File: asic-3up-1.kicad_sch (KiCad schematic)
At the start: 79 parts, among them J14 Conn_01x01, J15 Conn_01x01, J5 Conn_01x01, J7 Conn_01x01, U48 MCP1824T-1202E/OT, U49 MCP1824T-1202E/OT, U50 MCP1824T-1202E/OT, U51 MCP1824T-0802E, U52 MCP1824T-0802E, U53 MCP1824T-0802E, U54 BM1362AC_MODE1, U55 BM1362AC_MODE0, U56 BM1362AC_MODE1

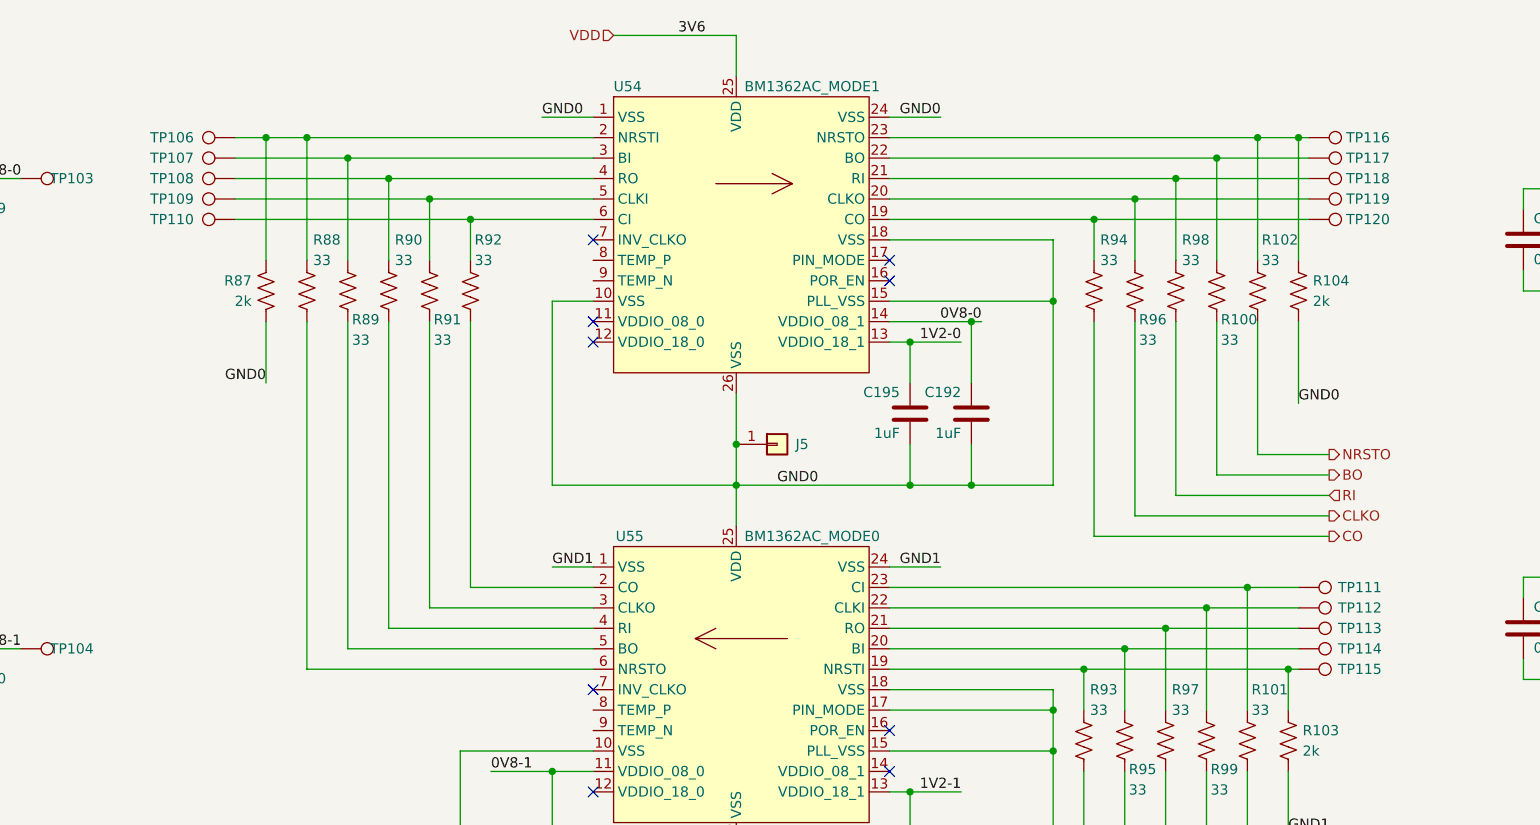
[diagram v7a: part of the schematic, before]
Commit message: all placed *almost* all routed
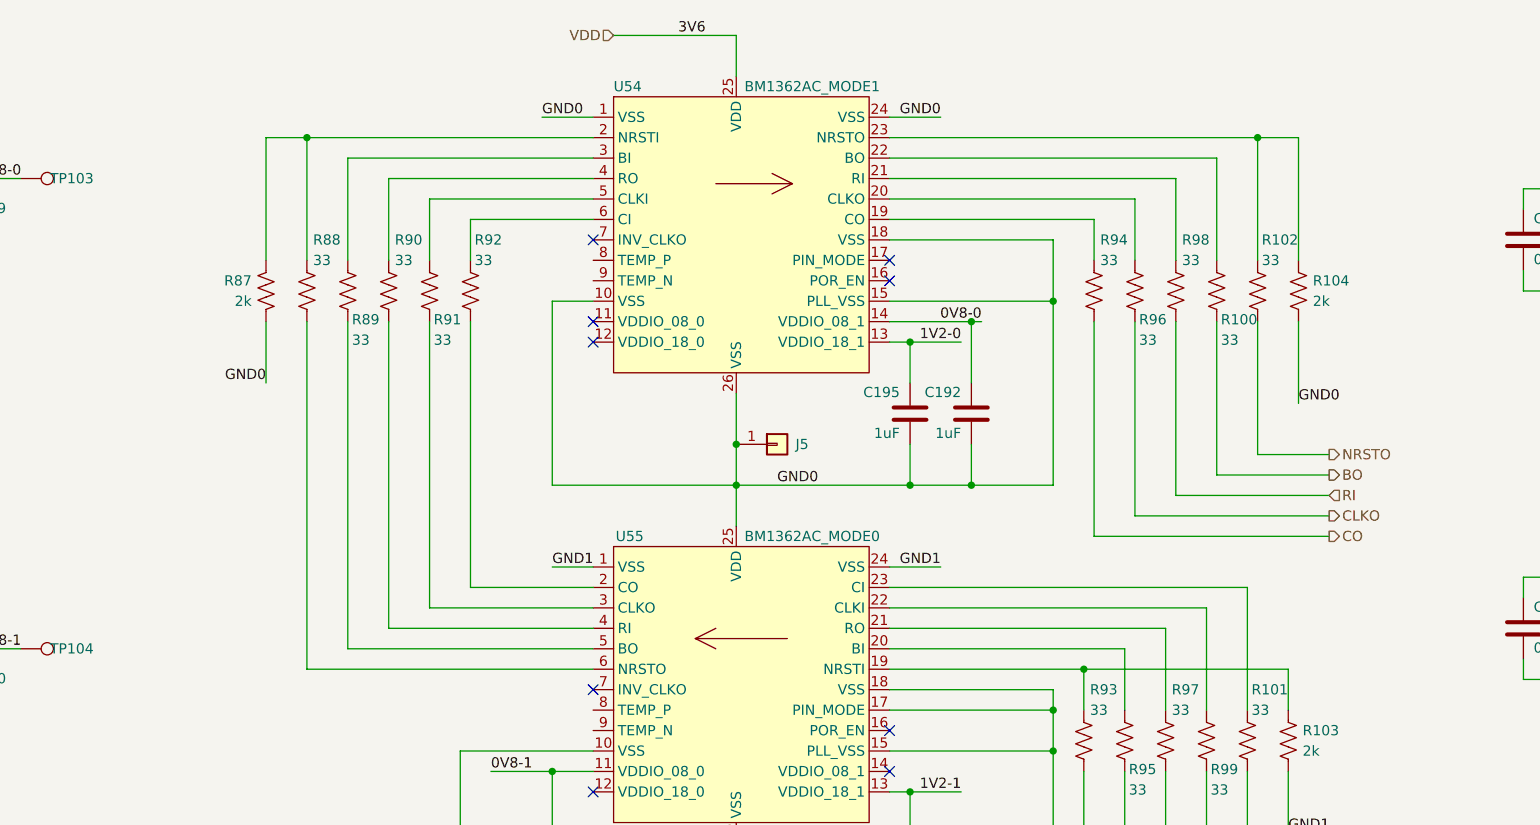
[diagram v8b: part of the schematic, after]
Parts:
- removed TP106, TP107, TP108, TP109, TP110, TP111, TP112, TP113, TP114, TP115, TP116, TP117, TP118, TP119, TP120: TestPoint, TestPoint:TestPoint_Pad_D1.0mm, symbol Connector:TestPoint
